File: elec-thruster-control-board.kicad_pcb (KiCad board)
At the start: 2 copper layers, 45 parts, among them J1 Conn_01x20_Socket, J10 Conn_01x02_Socket, J11 Conn_01x02_Socket, J13 Conn_02x05_Counter_Clockwise, J14 Conn_01x02_Socket, J2 Conn_01x02_Socket, J3 Conn_01x20_Socket, J4 Conn_01x02_Socket, J5 Conn_01x02_Socket, J6 Conn_01x02_Socket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

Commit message: Update 4:25 rewired to fit a pico footprint
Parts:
- removed J3: Conn_01x20_Socket, Connector_PinHeader_2.54mm:PinHeader_1x20_P2.54mm_Vertical_SMD_Pin1Left
- added A1: RaspberryPi_Pico, Module:RaspberryPi_Pico_Common_THT, F.Cu at (155.2, 30.1)
- moved J14 28.4 mm to (134.0, 54.5)
- moved D10 23.9 mm to (200.8, 35.8)
- moved D11 23.9 mm to (201.1, 94.8)
- moved D12 23.9 mm to (201.1, 86.5)
- moved D13 23.9 mm to (201.1, 78.5)
- moved D6 23.9 mm to (199.8, 69.2)
- moved D7 23.9 mm to (200.3, 60.8)
- moved D8 23.9 mm to (200.3, 52.2)
- moved D9 23.9 mm to (200.8, 44.0)
- moved J11 23.9 mm to (208.4, 35.0)
- moved J8 23.9 mm to (208.4, 69.5)
- moved R10 23.9 mm to (194.1, 35.5)
- moved R11 23.9 mm to (193.9, 94.0)
- moved R12 23.9 mm to (193.9, 86.0)
- moved R13 23.9 mm to (193.9, 78.0)
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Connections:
- D1 pad 1: Net-(D1-K) -> GND
- D11 pad 1: Net-(D11-K) -> GND
- D12 pad 1: Net-(D11-K) -> GND
- D13 pad 1: Net-(D11-K) -> GND
- D14 pad 1: Net-(D11-K) -> GND
- D15 pad 1: Net-(D11-K) -> GND
- D16 pad 1: Net-(D11-K) -> GND
- D2 pad 1: Net-(D2-K) -> GND
- D3 pad 1: Net-(D2-K) -> GND
- D4 pad 1: Net-(D4-K) -> GND
- D5 pad 1: Net-(D4-K) -> GND
- J13 pad 1: Net-(J13-Pin_1) -> unconnected-(J13-Pin_1-Pad1)
- J13 pad 2: Net-(J13-Pin_2) -> unconnected-(J13-Pin_2-Pad2)
- J13 pad 3: Net-(J13-Pin_3) -> unconnected-(J13-Pin_3-Pad3)
- J13 pad 4: Net-(J13-Pin_4) -> unconnected-(J13-Pin_4-Pad4)
- J13 pad 5: Net-(J13-Pin_5) -> unconnected-(J13-Pin_5-Pad5)
- J14 pad 1: Net-(D4-K) -> GND
- J2 pad 1: Net-(D1-K) -> GND
- J4 pad 1: Net-(D1-K) -> GND
- J5 pad 1: Net-(D2-K) -> GND
- J6 pad 1: Net-(D4-K) -> GND
- R1 pad 2: Net-(J13-Pin_1) -> Net-(A1-GPIO1)
- R2 pad 2: Net-(J13-Pin_2) -> Net-(A1-GPIO3)
- R3 pad 2: Net-(J13-Pin_3) -> Net-(A1-GPIO5)
- R4 pad 2: Net-(J13-Pin_4) -> Net-(A1-GPIO7)
- R5 pad 2: Net-(J13-Pin_5) -> Net-(A1-GPIO9)
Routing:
- net GND: track 0.00 -> 24.8 mm
- net Net-(J1-Pin_14): track 24.4 -> 0.00 mm
- net Net-(A1-GPIO4): track 0.00 -> 20.5 mm
- net Net-(A1-GPIO0): track 0.00 -> 19.4 mm
- net Net-(A1-GPIO2): track 0.00 -> 19.3 mm
- net Net-(A1-GPIO7): track 0.00 -> 11.4 mm
- net Net-(A1-GPIO5): track 0.00 -> 6.20 mm
- net Net-(A1-GPIO1): track 0.00 -> 4.88 mm
- net Net-(A1-GPIO3): track 0.00 -> 4.83 mm
- net Net-(D3-A): track 0.00 -> 4.28 mm
- net Net-(D2-A): track 0.00 -> 4.28 mm
- net Net-(D4-A): track 0.00 -> 4.23 mm
- net Net-(D1-A): track 0.00 -> 4.18 mm
- net Net-(A1-GPIO8): track 0.00 -> 4.13 mm

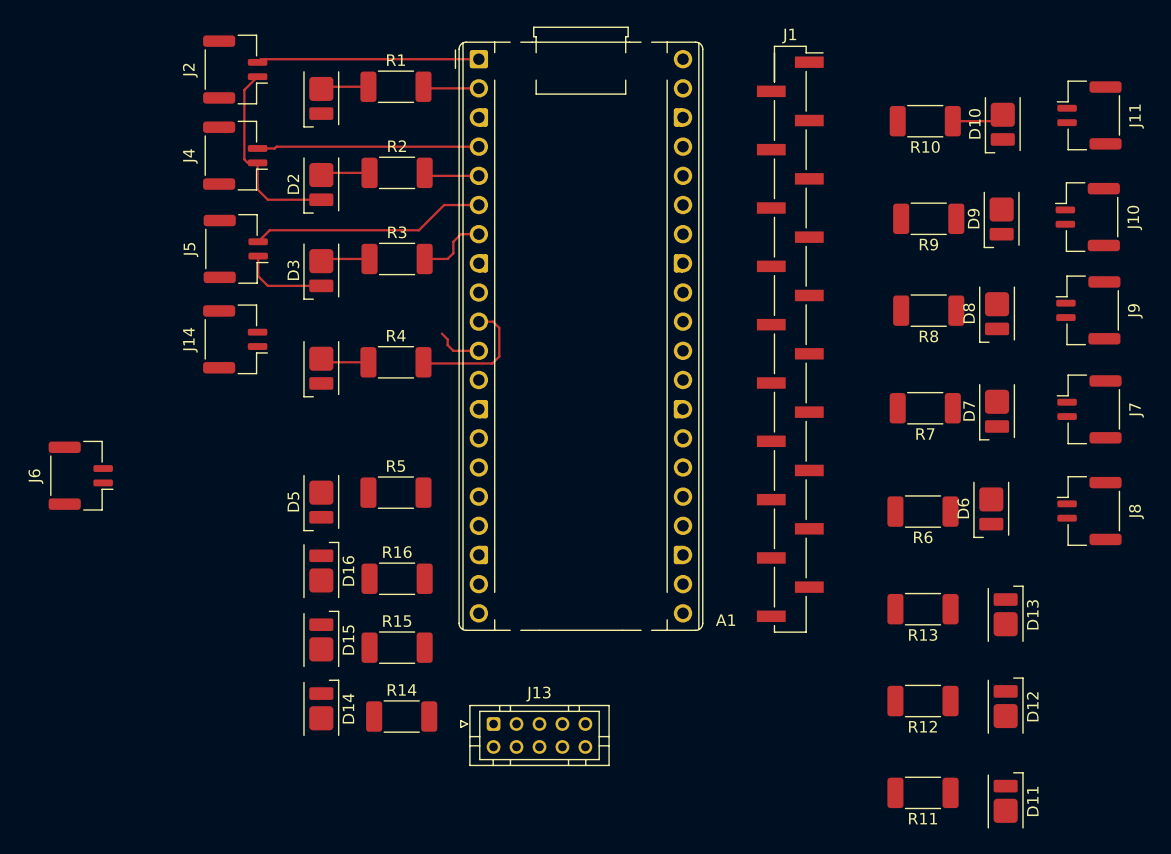
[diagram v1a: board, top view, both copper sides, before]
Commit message: I fixed it such that the board now accurately fits a Pi Pico
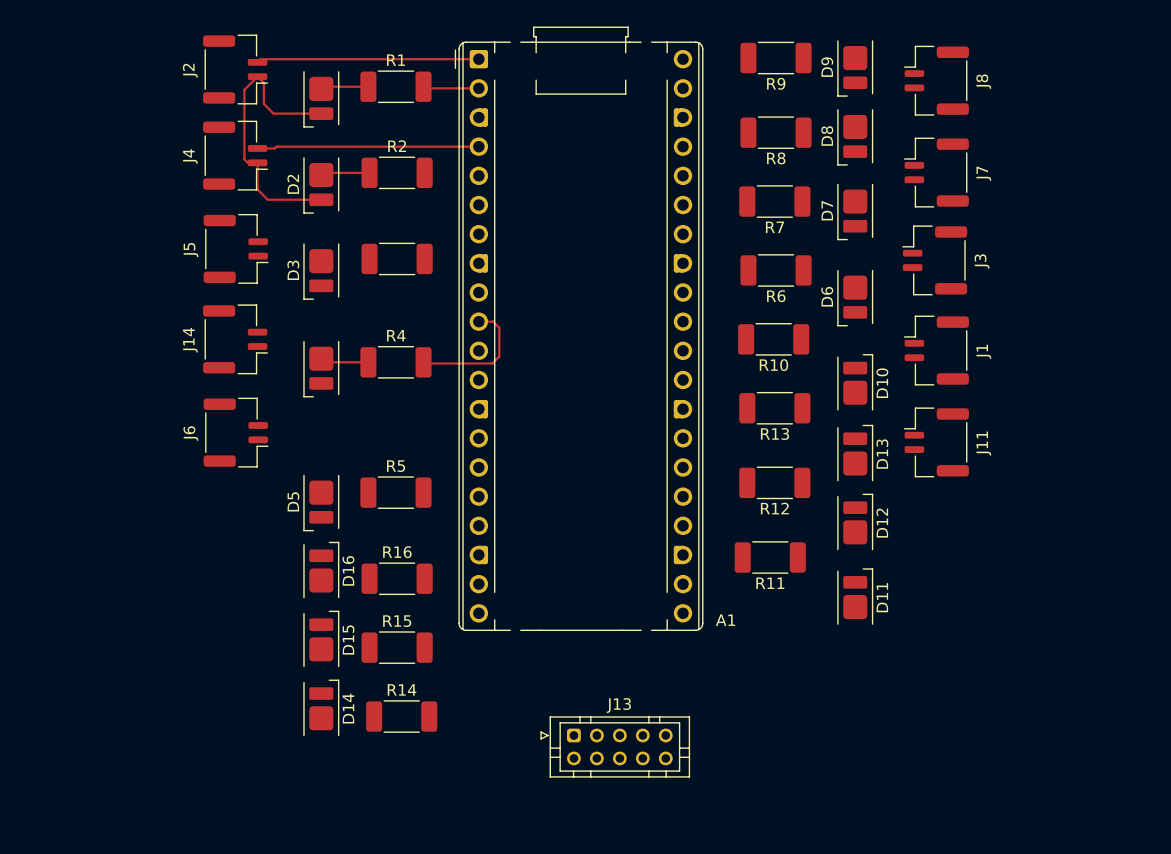
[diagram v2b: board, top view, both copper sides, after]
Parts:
- removed J10, J9: Conn_01x02_Socket, Connector_JST:JST_GH_BM02B-GHS-TBT_1x02-1MP_P1.25mm_Vertical
- added J3: Conn_01x02_Socket, Connector_JST:JST_GH_BM02B-GHS-TBT_1x02-1MP_P1.25mm_Vertical, F.Cu at (194.9, 47.6)
- J1: value Conn_01x20_Socket -> Conn_01x02_Socket; footprint Connector_PinHeader_2.54mm:PinHeader_1x20_P2.54mm_Vertical_SMD_Pin1Right -> Connector_JST:JST_GH_BM02B-GHS-TBT_1x02-1MP_P1.25mm_Vertical
- moved J8 39.8 mm to (195.1, 32.0)
- moved J11 31.4 mm to (195.1, 63.5)
- moved D10 26.0 mm to (188.0, 58.3), turned to -90 degrees
- moved R6 24.6 mm to (181.1, 48.5)
- moved J7 24.5 mm to (195.1, 40.0)
- moved R11 24.4 mm to (180.6, 73.5)
- moved R10 23.1 mm to (180.9, 54.5)
- moved R12 23.0 mm to (181.0, 67.0)
- moved R7 22.3 mm to (181.0, 42.5)
- moved D11 22.1 mm to (188.0, 77.0)
- moved D6 21.9 mm to (188.0, 50.8)
- moved R13 21.7 mm to (181.0, 60.5)
- moved D7 21.4 mm to (188.0, 43.3)
- moved D12 20.7 mm to (188.0, 70.5)
- moved R8 20.4 mm to (181.1, 36.5)
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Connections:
- A1 pad 21: unconnected-(A1-GPIO16-Pad21) -> Net-(A1-GPIO16)
- A1 pad 22: unconnected-(A1-GPIO17-Pad22) -> Net-(A1-GPIO17)
- A1 pad 24: unconnected-(A1-GPIO18-Pad24) -> Net-(A1-GPIO18)
- A1 pad 25: unconnected-(A1-GPIO19-Pad25) -> Net-(A1-GPIO19)
- A1 pad 26: unconnected-(A1-GPIO20-Pad26) -> Net-(A1-GPIO20)
- A1 pad 27: unconnected-(A1-GPIO21-Pad27) -> Net-(A1-GPIO21)
- A1 pad 29: unconnected-(A1-GPIO22-Pad29) -> Net-(A1-GPIO22)
- A1 pad 31: unconnected-(A1-GPIO26_ADC0-Pad31) -> Net-(A1-GPIO26_ADC0)
- A1 pad 32: unconnected-(A1-GPIO27_ADC1-Pad32) -> Net-(A1-GPIO27_ADC1)
- A1 pad 34: unconnected-(A1-GPIO28_ADC2-Pad34) -> Net-(A1-GPIO28_ADC2)
- D10 pad 1: Net-(D10-K) -> GND
- D6 pad 1: Net-(D6-K) -> GND
- D7 pad 1: Net-(D7-K) -> GND
- D8 pad 1: Net-(D6-K) -> GND
- D9 pad 1: Net-(D7-K) -> GND
- J1 pad 1: Net-(J1-Pin_1) -> GND
- J1 pad 2: Net-(J1-Pin_2) -> Net-(A1-GPIO18)
- J11 pad 1: Net-(J1-Pin_14) -> GND
- J11 pad 2: Net-(D10-K) -> Net-(A1-GPIO16)
- J13 pad 1: unconnected-(J13-Pin_1-Pad1) -> Net-(A1-GPIO0)
- J13 pad 10: Net-(J1-Pin_1) -> Net-(A1-GPIO27_ADC1)
- J13 pad 2: unconnected-(J13-Pin_2-Pad2) -> Net-(A1-GPIO2)
- J13 pad 3: unconnected-(J13-Pin_3-Pad3) -> Net-(A1-GPIO4)
- J13 pad 4: unconnected-(J13-Pin_4-Pad4) -> Net-(A1-GPIO6)
- J13 pad 5: unconnected-(J13-Pin_5-Pad5) -> Net-(A1-GPIO8)
- J13 pad 6: Net-(J1-Pin_12) -> Net-(A1-GPIO16)
- J13 pad 7: Net-(J1-Pin_9) -> Net-(A1-GPIO18)
- J13 pad 8: Net-(J1-Pin_6) -> Net-(A1-GPIO20)
- J13 pad 9: Net-(J1-Pin_4) -> Net-(A1-GPIO22)
- J7 pad 1: Net-(J1-Pin_2) -> GND
- J7 pad 2: Net-(D6-K) -> Net-(A1-GPIO22)
- J8 pad 1: Net-(J1-Pin_5) -> GND
- J8 pad 2: Net-(D6-K) -> Net-(A1-GPIO27_ADC1)
- R10 pad 2: Net-(J1-Pin_12) -> Net-(A1-GPIO17)
- R6 pad 2: Net-(J1-Pin_1) -> Net-(A1-GPIO19)
- R7 pad 2: Net-(J1-Pin_6) -> Net-(A1-GPIO21)
- R8 pad 2: Net-(J1-Pin_4) -> Net-(A1-GPIO26_ADC0)
- R9 pad 2: Net-(J1-Pin_9) -> Net-(A1-GPIO28_ADC2)
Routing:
- net Net-(A1-GPIO4): track 20.5 -> 0.00 mm
- net Net-(A1-GPIO5): track 6.20 -> 0.00 mm
- net Net-(A1-GPIO3): track 4.83 -> 0.37 mm
- net Net-(A1-GPIO8): track 4.13 -> 0.00 mm
- net Net-(D10-A): track 4.08 -> 0.00 mm
- net Net-(D3-A): track 4.28 -> 0.27 mm

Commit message: needs work on the traces
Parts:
- moved D13 65.8 mm to (122.5, 71.0)
- moved R16 56.9 mm to (205.0, 73.0)
- moved D14 56.9 mm to (198.4, 85.8), turned to 90 degrees
- moved D15 56.9 mm to (198.4, 79.8), turned to 90 degrees
- moved D16 56.9 mm to (198.4, 73.8), turned to 90 degrees
- moved R13 48.7 mm to (133.6, 71.5)
- moved R14 17.4 mm to (148.0, 70.0)
- moved R15 5.85 mm to (148.0, 75.5)
- moved D5 3.85 mm to (141.5, 64.8)
- moved R5 3.85 mm to (148.0, 64.0)
- moved J11 1.00 mm to (195.1, 64.5)
- moved J1 0.15 mm to (195.1, 55.6)
- moved J3 0.05 mm to (195.0, 47.6)
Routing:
- net GND: track 25.1 -> 183.0 mm, vias 0 -> 24
- net Net-(A1-GPIO6): track 0.00 -> 68.0 mm
- net Net-(A1-GPIO0): track 19.4 -> 82.1 mm
- net Net-(A1-GPIO20): track 0.00 -> 57.8 mm
- net Net-(A1-GPIO22): track 0.00 -> 48.9 mm
- net Net-(A1-GPIO16): track 0.00 -> 35.6 mm
- net Net-(A1-GPIO27_ADC1): track 0.00 -> 34.8 mm
- net Net-(A1-GPIO4): track 0.00 -> 33.2 mm
- net Net-(A1-GPIO15): track 0.00 -> 29.1 mm, vias 0 -> 2
- net Net-(A1-GPIO10): track 0.00 -> 27.1 mm, vias 0 -> 2
- net Net-(A1-GPIO17): track 0.00 -> 23.7 mm
- net Net-(A1-GPIO8): track 0.00 -> 23.4 mm
- net Net-(A1-GPIO21): track 0.00 -> 22.9 mm
- net Net-(A1-GPIO19): track 0.00 -> 22.8 mm
- net Net-(A1-GPIO28_ADC2): track 0.00 -> 20.4 mm
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
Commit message: hi this is the work I did thursday
This is the work I did on Thursday.
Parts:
- moved R16 74.6 mm to (141.3, 111.9)
- moved D16 73.9 mm to (134.9, 111.7), turned to -90 degrees
- moved D12 70.7 mm to (134.9, 117.2)
- moved D11 70.1 mm to (134.9, 122.7)
- moved D15 68.6 mm to (134.9, 105.9)
- moved D14 65.1 mm to (134.9, 100.1)
- moved R12 64.5 mm to (141.4, 117.9), turned to 0 degrees
- moved R11 63.8 mm to (141.4, 123.9), turned to 0 degrees
- moved R6 31.9 mm to (179.4, 80.4)
- moved R7 31.9 mm to (179.4, 74.4)
- moved R10 31.9 mm to (179.4, 86.4)
- moved R8 31.4 mm to (179.5, 67.9)
- moved R9 31.4 mm to (179.5, 61.4)
- moved R15 31.1 mm to (141.4, 105.9)
- moved R14 30.6 mm to (141.5, 99.9)
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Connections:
- J1 pad 2: Net-(A1-GPIO18) -> Net-(A1-GPIO16)
- J11 pad 2: Net-(A1-GPIO16) -> Net-(A1-GPIO18)
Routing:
- net Net-(A1-GPIO0): track 82.1 -> 25.8 mm
- net Net-(A1-GPIO6): track 68.0 -> 23.1 mm
- net GND: track 183.0 -> 225.0 mm, vias 24 -> 28
- net Net-(A1-GPIO18): track 0.00 -> 37.7 mm
- net Net-(A1-GPIO13): track 0.00 -> 22.4 mm
- net Net-(A1-GPIO14): track 3.04 -> 23.5 mm, vias 1 -> 0
- net Net-(A1-GPIO12): track 0.00 -> 19.1 mm
- net Net-(A1-GPIO20): track 57.8 -> 40.4 mm
- net Net-(A1-GPIO10): track 27.1 -> 11.2 mm, vias 2 -> 0
- net Net-(A1-GPIO11): track 0.00 -> 14.9 mm
- net Net-(A1-GPIO4): track 33.2 -> 21.4 mm
- net Net-(A1-GPIO22): track 48.9 -> 39.2 mm
- net Net-(D11-A): track 8.84 -> 4.24 mm
- net (no net): track 0.00 -> 4.50 mm
- net Net-(D14-A): track 0.00 -> 4.47 mm
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
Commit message: Add files via upload
Major MAJOR changes to everything. Added variable wire thicknesses and fixed a lot of things.
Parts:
- removed J1, J14, J3, J4, J6, J7, J8: Conn_01x02_Socket, Connector_JST:JST_GH_BM02B-GHS-TBT_1x02-1MP_P1.25mm_Vertical
- added J12: Conn_01x02_Socket, Connector_JST:JST_PH_B2B-PH-SM4-TB_1x02-1MP_P2.00mm_Vertical, F.Cu at (125.8, 64.9)
- added J15: Conn_01x02_Socket, Connector_JST:JST_PH_B2B-PH-SM4-TB_1x02-1MP_P2.00mm_Vertical, F.Cu at (126.0, 85.1)
- added J16: Conn_01x02_Socket, Connector_JST:JST_PH_B2B-PH-SM4-TB_1x02-1MP_P2.00mm_Vertical, F.Cu at (126.2, 95.2)
- added J18: Conn_01x02_Socket, Connector_JST:JST_PH_B2B-PH-SM4-TB_1x02-1MP_P2.00mm_Vertical, F.Cu at (190.0, 96.8)
- added J19: Conn_01x02_Socket, Connector_JST:JST_PH_B2B-PH-SM4-TB_1x02-1MP_P2.00mm_Vertical, F.Cu at (190.0, 86.2)
- added J20: Conn_01x02_Socket, Connector_JST:JST_PH_B2B-PH-SM4-TB_1x02-1MP_P2.00mm_Vertical, F.Cu at (190.0, 75.2)
- added J21: Conn_01x02_Socket, Connector_JST:JST_PH_B2B-PH-SM4-TB_1x02-1MP_P2.00mm_Vertical, F.Cu at (190.0, 64.5)
- J11, J2, J5: footprint Connector_JST:JST_GH_BM02B-GHS-TBT_1x02-1MP_P1.25mm_Vertical -> Connector_JST:JST_PH_B2B-PH-SM4-TB_1x02-1MP_P2.00mm_Vertical
- J13: moved to B.Cu
- moved J11 29.9 mm to (190.2, 108.1)
- moved R10 14.0 mm to (174.5, 99.5)
- moved D10 12.9 mm to (181.5, 98.8)
- moved D6 12.7 mm to (181.5, 91.3)
- moved R6 12.6 mm to (174.6, 92.0)
- moved D7 12.3 mm to (181.5, 84.7)
- moved R11 12.0 mm to (143.0, 112.0), turned to 90 degrees
- moved R7 11.6 mm to (174.6, 85.0)
- moved D8 11.6 mm to (181.5, 77.5), turned to 90 degrees
- moved R16 10.8 mm to (130.5, 112.0), turned to 90 degrees
- moved D13 10.3 mm to (129.7, 103.0), turned to 0 degrees
- moved D9 10.1 mm to (181.5, 69.8), turned to 90 degrees
- moved R13 10.00 mm to (132.5, 97.8), turned to 90 degrees
- moved R8 9.90 mm to (174.6, 76.5)
- moved R9 9.10 mm to (174.5, 69.0)
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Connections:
- net Net-(A1-GPIO0) renamed /gpio0
- net Net-(A1-GPIO2) renamed /gpio2
- net Net-(A1-GPIO20) renamed /gpio20
- net Net-(A1-GPIO22) renamed /gpio22
- net Net-(A1-GPIO4) renamed /gpio4
- net Net-(A1-GPIO6) renamed /gpio6
- A1 pad 11: Net-(A1-GPIO8) -> /gpio8
- A1 pad 21: Net-(A1-GPIO16) -> /gpio16
- A1 pad 24: Net-(A1-GPIO18) -> /gpio18
- A1 pad 32: Net-(A1-GPIO27_ADC1) -> /gpio9_pwm9
- J11 pad 2: Net-(A1-GPIO18) -> /gpio16
- J13 pad 10: Net-(A1-GPIO27_ADC1) -> GND
- J13 pad 5: Net-(A1-GPIO8) -> /CLK
- J13 pad 6: Net-(A1-GPIO16) -> /gpio16
- J13 pad 7: Net-(A1-GPIO18) -> /gpio18
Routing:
- net GND: track 225.0 -> 329.2 mm, vias 28 -> 30
- net Net-(A1-GND-Pad13): track 17.8 -> 106.7 mm
- net /gpio2: track 19.3 -> 80.8 mm
- net /gpio4: track 21.4 -> 81.0 mm
- net /gpio0: track 25.8 -> 83.7 mm
- net /gpio6: track 23.1 -> 77.1 mm
- net /gpio18: track 0.00 -> 53.4 mm
- net /gpio16: track 0.00 -> 52.2 mm
- net Net-(A1-GPIO27_ADC1): track 38.6 -> 0.00 mm
- net Net-(A1-GPIO16): track 37.7 -> 0.00 mm
- net Net-(A1-GPIO18): track 37.7 -> 0.00 mm
- net /gpio8: track 0.00 -> 31.9 mm
- net /gpio9_pwm9: track 0.00 -> 29.3 mm
- net Net-(A1-GPIO8): track 23.4 -> 0.00 mm
- net /gpio22: track 39.2 -> 61.6 mm
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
